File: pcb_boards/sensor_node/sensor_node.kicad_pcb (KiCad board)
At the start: 2 copper layers, 77 x 77 mm, 65 parts, among them IC1 PCF2129AT, J1 Conn_02x03_Counter_Clockwise, J2 Conn_01x02, J3 USB_B_Micro, J4 Conn_01x02, J5 Conn_01x02, U1 SiP32431, U2 ESP32-WROOM-32, U3 RF-LORA-868-SO, U5 SHTC3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

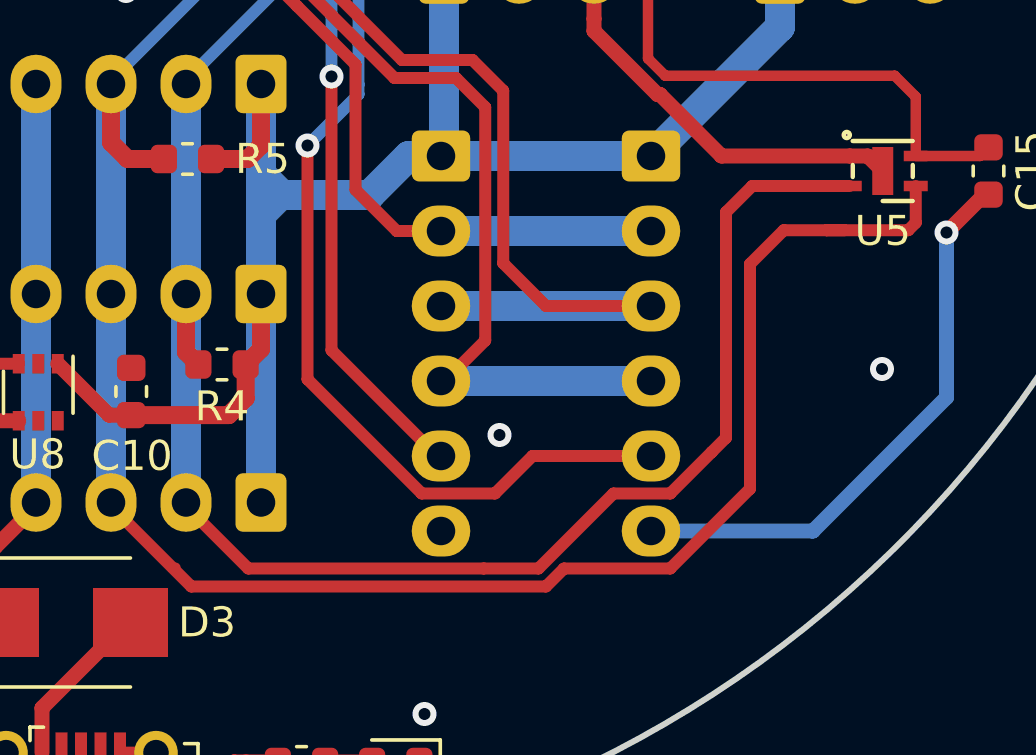
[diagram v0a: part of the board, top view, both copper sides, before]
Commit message: Add firmware and update PCBs
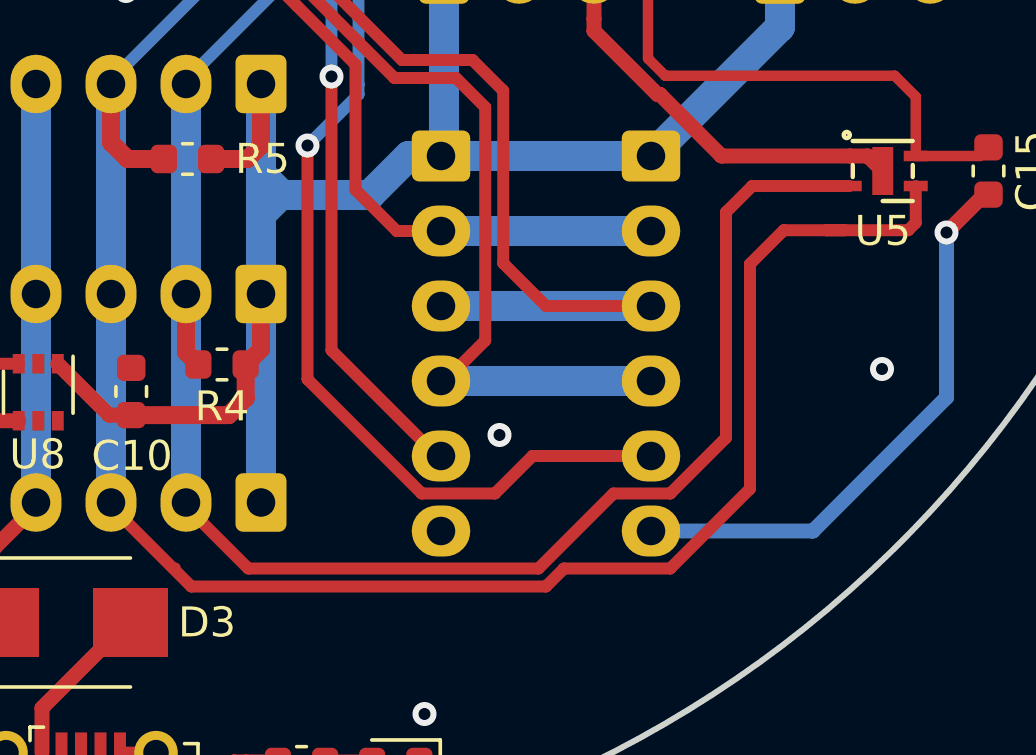
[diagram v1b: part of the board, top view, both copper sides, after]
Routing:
- net /SCL: track 138.4 -> 136.2 mm
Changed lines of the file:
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@@
     (thickness 1.6)
     (drawings 41)
-    (tracks 877)
+    (tracks 872)
     (zones 0)
     (modules 65)
@@
   (segment (start 102.95001 73.74999) (end 103.915 72.785) (width 0.4) (layer F.Cu) (net 2))
   (segment (start 105.45001 128.07501) (end 103.4 126.025) (width 0.35) (layer F.Cu) (net 2))
-  (segment (start 125.525 115.35) (end 124.075 115.35) (width 0.35) (layer F.Cu) (net 2))
-  (segment (start 121.40001 116.22499) (end 122.275 115.35) (width 0.4) (layer F.Cu) (net 2))
   (segment (start 103.4 126.025) (end 103.4 125.9) (width 0.4) (layer F.Cu) (net 2))
-  (segment (start 105.47501 128.10001) (end 103.4 126.025) (width 0.4) (layer F.Cu) (net 2))
-  (segment (start 113.325 128.10001) (end 115.14999 128.10001) (width 0.4) (layer F.Cu) (net 2))
-  (segment (start 113.325 128.10001) (end 105.47501 128.10001) (width 0.4) (layer F.Cu) (net 2))
-  (segment (start 115.14999 128.10001) (end 117.65 125.6) (width 0.4) (layer F.Cu) (net 2))
-  (segment (start 117.65 125.6) (end 119.542781 125.6) (width 0.4) (layer F.Cu) (net 2))
-  (segment (start 121.40001 123.742771) (end 120.925 124.217781) (width 0.4) (layer F.Cu) (net 2))
-  (segment (start 121.40001 121.05) (end 121.40001 123.742771) (width 0.4) (layer F.Cu) (net 2))
-  (segment (start 121.40001 121.05) (end 121.40001 116.22499) (width 0.4) (layer F.Cu) (net 2))
-  (segment (start 119.542781 125.6) (end 120.925 124.217781) (width 0.4) (layer F.Cu) (net 2))
-  (segment (start 123.3 115.35) (end 125.525 115.35) (width 0.4) (layer F.Cu) (net 2))
-  (segment (start 123.3 115.35) (end 124.075 115.35) (width 0.4) (layer F.Cu) (net 2))
-  (segment (start 122.275 115.35) (end 123.3 115.35) (width 0.4) (layer F.Cu) (net 2))
   (via (at 84.15 93.55) (size 0.8) (drill 0.4) (layers F.Cu B.Cu) (net 2))
   (segment (start 84.85 92.85) (end 84.15 93.55) (width 0.4) (layer B.Cu) (net 2))
@@
   (segment (start 74.585 91.175685) (end 75.059316 91.650001) (width 0.4) (layer F.Cu) (net 2))
   (segment (start 74.585 90.5) (end 74.585 91.175685) (width 0.4) (layer F.Cu) (net 2))
+  (segment (start 124.075 115.35) (end 125.525 115.35) (width 0.4) (layer F.Cu) (net 2))
+  (segment (start 121.40001 116.22499) (end 122.275 115.35) (width 0.4) (layer F.Cu) (net 2))
+  (segment (start 115.14999 128.10001) (end 117.65 125.6) (width 0.4) (layer F.Cu) (net 2))
+  (segment (start 119.542781 125.6) (end 121.40001 123.742771) (width 0.4) (layer F.Cu) (net 2))
+  (segment (start 103.4 126.025) (end 105.47501 128.10001) (width 0.4) (layer F.Cu) (net 2))
+  (segment (start 122.275 115.35) (end 124.075 115.35) (width 0.4) (layer F.Cu) (net 2))
+  (segment (start 105.47501 128.10001) (end 115.14999 128.10001) (width 0.4) (layer F.Cu) (net 2))
+  (segment (start 117.65 125.6) (end 119.542781 125.6) (width 0.4) (layer F.Cu) (net 2))
+  (segment (start 121.40001 123.742771) (end 121.40001 116.22499) (width 0.4) (layer F.Cu) (net 2))
   (segment (start 100.9 113.9) (end 101.45 114.45) (width 0.6) (layer F.Cu) (net 3))
   (segment (start 101.45 114.45) (end 102.6625 114.45) (width 0.6) (layer F.Cu) (net 3))

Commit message: Update PCB.
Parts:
- added AE2: Antenna, RF_Antenna:Texas_SWRA416_868MHz_915MHz, F.Cu at (83.8, 45.9)
- added C1: 1pF, Capacitor_SMD:C_0603_1608Metric, F.Cu at (118.3, 109.3)
- added JP1: Jumper_3_Open, Jumper:SolderJumper-3_P1.3mm_Open_Pad1.0x1.5mm, F.Cu at (74.9, 58.4)
- added L2: 12nH, Inductor_SMD:L_0603_1608Metric, F.Cu at (122.3, 110.1)
- R10, R12: value R4.7k -> 4.7k
- moved ANT1 109.6 mm to (177.3, 102.3)
- moved C16 109.6 mm to (190.9, 118.8)
- moved C18 109.6 mm to (190.9, 121.2)
- moved IC1 109.6 mm to (189.8, 80.6)
- moved J1 109.6 mm to (227.1, 94.3)
- moved J4 109.6 mm to (223.0, 65.7)
- moved OWI1 109.6 mm to (212.3, 95.5)
- moved OWI2 109.6 mm to (205.3, 95.5)
- moved R12 109.6 mm to (207.6, 96.8)
- moved R2 109.6 mm to (190.3, 73.4)
- moved R9 109.6 mm to (203.8, 87.8)
- moved AE1 109.6 mm to (180.0, 94.9)
- moved BT2 109.6 mm to (222.0, 94.7)
- moved BT3 109.6 mm to (206.5, 83.3)
- moved C11 109.6 mm to (204.1, 117.3)
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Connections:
- ANT1 pad 1: Net-(AE1-Pad1) -> Net-(ANT1-Pad1)
- U2 pad 39: (no net) -> GND
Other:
- board size 77 x 77 mm -> 209.5 x 94.6 mm
- rule pad_to_mask_clearance: 0.051 -> 0

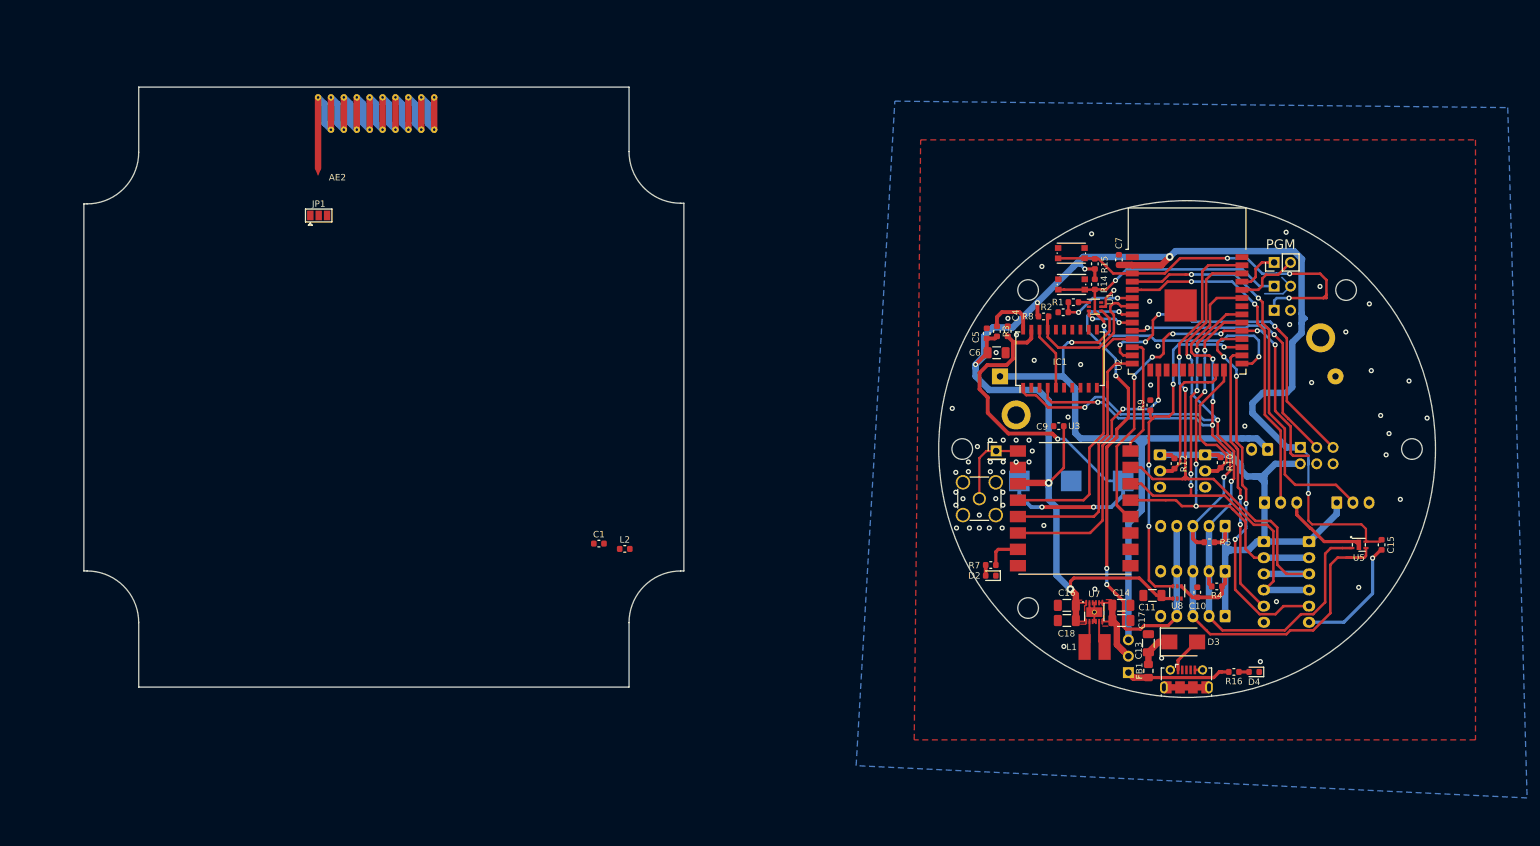
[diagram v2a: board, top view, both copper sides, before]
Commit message: New routing design.
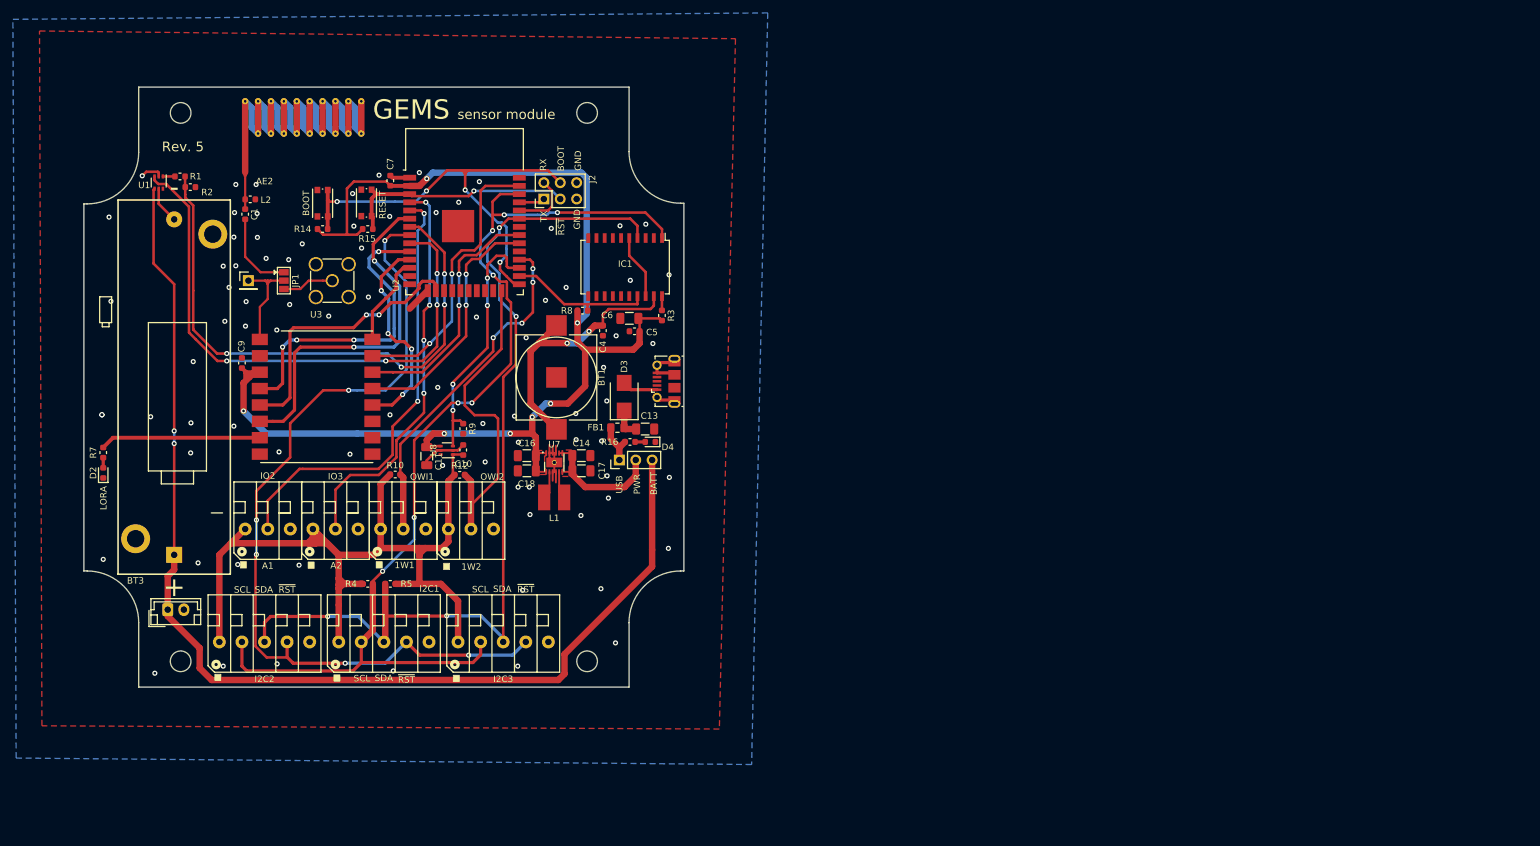
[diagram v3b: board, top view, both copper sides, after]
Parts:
- removed C15: 100nF, Capacitor_SMD:C_0603_1608Metric
- removed H7: MountingHole, MountingHole:MountingHole_3.2mm_M3
- removed J1: Conn_02x03_Counter_Clockwise, Connector_PinHeader_2.54mm:PinHeader_2x03_P2.54mm_Vertical
- removed J4, J5: Conn_01x02, Connector_PinHeader_2.54mm:PinHeader_1x02_P2.54mm_Vertical
- removed SPI1, SPI2: Conn_01x06, Connector_JST:JST_XH_B06B-XH-A_1x06_P2.50mm_Vertical
- removed U5: SHTC3, gems_footprints:DFN_4_Pin_2x2mm
- BT1, BT2, BT3, JP2: moved to F.Cu
- I2C1, I2C2, I2C3: footprint Connector_JST:JST_XH_B05B-XH-A_1x05_P2.50mm_Vertical -> gems_footprints:TerminalBlock_Phoenix_PTSA-1,2-2-3,5-F-THR-1x05-P3.50mm_45Degree; moved to F.Cu
- IO2, IO3, OWI1, OWI2: footprint Connector_JST:JST_XH_B03B-XH-A_1x03_P2.50mm_Vertical -> gems_footprints:TerminalBlock_Phoenix_PTSA-1,2-2-3,5-F-THR-1x03-P3.50mm_45Degree; moved to F.Cu
- IO4: value BOOT OPTION -> BOOT
- J2: value Conn_01x02 -> Conn_02x03_Odd_Even; footprint Connector_PinHeader_2.54mm:PinHeader_1x02_P2.54mm_Vertical -> Connector_PinHeader_2.54mm:PinHeader_2x03_P2.54mm_Vertical; moved to F.Cu
- moved H3 197.8 mm to (53.5, 42.5)
- moved H4 189.6 mm to (53.5, 127.5)
- moved BT2 172.3 mm to (51.5, 119.5), turned to 0 degrees
- moved IO3 155.3 mm to (77.5, 107.0)
- moved IO2 154.6 mm to (67.0, 107.0)
- moved BT3 154.0 mm to (52.5, 85.0), turned to 90 degrees
- moved I2C2 150.0 mm to (66.5, 124.5), turned to 0 degrees
- moved U1 146.4 mm to (50.1, 53.3), turned to 270 degrees
- moved R1 139.8 mm to (53.4, 52.4), turned to 180 degrees
- moved R7 138.7 mm to (41.5, 95.2), turned to 90 degrees
- moved D2 138.5 mm to (41.5, 98.3), turned to 90 degrees
- moved R2 136.7 mm to (55.0, 54.0), turned to 0 degrees
- moved R4 131.6 mm to (82.5, 115.5), turned to 180 degrees
- moved I2C1 130.5 mm to (85.0, 124.5), turned to 0 degrees
- moved R10 128.0 mm to (86.8, 98.5), turned to 0 degrees
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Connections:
- J2 pad 1: /BOOT -> /TX
- J2 pad 2: GND -> /RX
- U2 pad 10: /DAC -> /RX_SW
- U2 pad 11: /RX_SW -> /~RST_RF
- U2 pad 13: /D1 -> Net-(U2-Pad13)
- U2 pad 14: /TX_SW -> Net-(U2-Pad14)
- U2 pad 16: /IRQ -> /TX_SW
- U2 pad 23: /ONE_W2 -> Net-(U2-Pad23)
- U2 pad 24: /ONE_W1 -> /ONE_W2
- U2 pad 26: /~CS1 -> /INT_T
- U2 pad 28: /~CS2 -> /ONE_W1
- U2 pad 29: /~RST_RF -> Net-(U2-Pad29)
- U2 pad 6: /BATT_M -> /IRQ
- U2 pad 7: /INT_T -> /BATT_M
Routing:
- net /BATT_MC: track 7.88 -> 87.9 mm, vias 2 -> 4
- net /BATT_M: track 12.4 -> 88.4 mm, vias 2 -> 4
- net +BATT: track 101.7 -> 174.8 mm, vias 1 -> 2
- net /~CS2: track 58.4 -> 0.00 mm, vias 4 -> 0
- net /D1: track 54.7 -> 0.00 mm, vias 4 -> 0
- net /~RST_I2C: track 84.0 -> 132.4 mm, vias 4 -> 6
- net +3V3: track 240.7 -> 194.4 mm
- net VPP: track 94.5 -> 139.3 mm
- net /MOSI: track 87.3 -> 44.1 mm
- net /DAC: track 43.1 -> 0.00 mm, vias 2 -> 0
- net /~CS1: track 42.6 -> 0.00 mm, vias 2 -> 0
- net /~RST_RF: track 71.8 -> 32.4 mm, vias 6 -> 4
- net /MISO: track 74.8 -> 38.4 mm, vias 4 -> 2
- net /ONE_W1: track 22.3 -> 53.6 mm, vias 0 -> 4
- net /ONE_W2: track 22.9 -> 53.8 mm
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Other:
- board size 209.5 x 94.6 mm -> 93 x 93 mm
- board text added: "BOOT"
- board text added: "GND"
- board text added: "LORA"
- board text added: "PWR"
- board text added: "RX"
- board text added: "Rev. 5"
- board text added: "SCL"
- board text added: "SDA"
- board text added: "TX"
- board text added: "~RST"
- board text removed: "BT"
- board text removed: "EXP"
- board text removed: "I2C"
- board text removed: "PGM"
- board text removed: "POWER"
- board text removed: "RST"
- board text removed: "Rev. 4"
- board text removed: "SPI1"
- board text removed: "SPI2"
- board text removed: "USER"
